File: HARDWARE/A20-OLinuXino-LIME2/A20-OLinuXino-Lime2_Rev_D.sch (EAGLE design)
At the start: 421 parts, among them Q1 E4SB25.000F20E15(25MHz/20pF/2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, Q3 4SB24.000F20E15/5x3.2mm/20ppm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, Q4 32768Hz/6pF, T1 BC846B, U1 A20, U10 SY6280, U11 SY6280, U12 SY6280, U13 AXP209(QFN48), U14 MCP120T475I-TT, U15 SY8008C(AA)C, U16 SY7208(SOT23-6), U17 SY8008C(AA)C, U18 FIDUCIAL, U19 FIDUCIAL, U2 K4B4G1646D-BCK0, U20 FIDUCIAL, U21 FIDUCIAL, U3 K4B4G1646D-BCK0, U4 H27UBG8T2BTR, U5 RTL8211CL-GR, U6 AT24C16BN-SH, U7 NA(RCLAMP0524P), U8 NA(RCLAMP0524P), U9 NA(RCLAMP0524P)

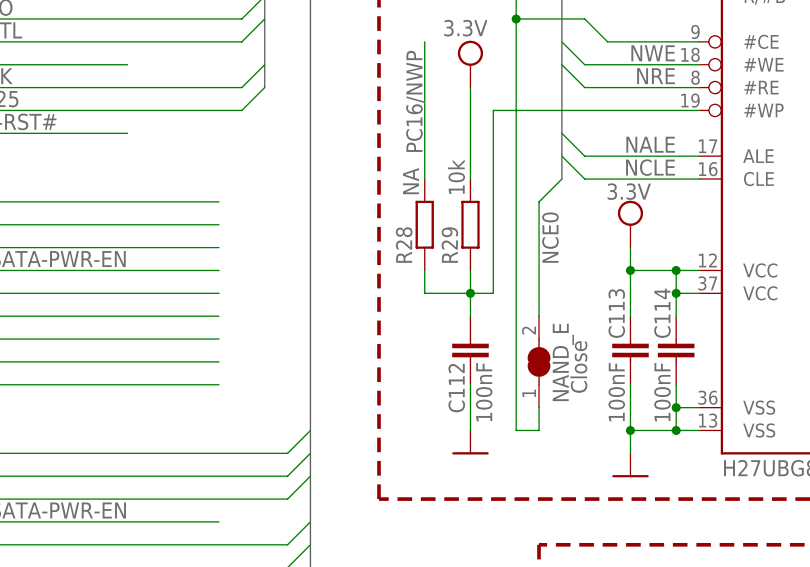
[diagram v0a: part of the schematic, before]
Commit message: Rename R28 to NAND_WP
R28 is a spot where a zero ohm resistor can be placed to control the
NAND flash's Write Protect. This commit renames this resistor to NAND_WP
and marks it as such on the silk-screen.

Signed-off-by: Olliver Schinagl <o.schinagl@ultimaker.com>
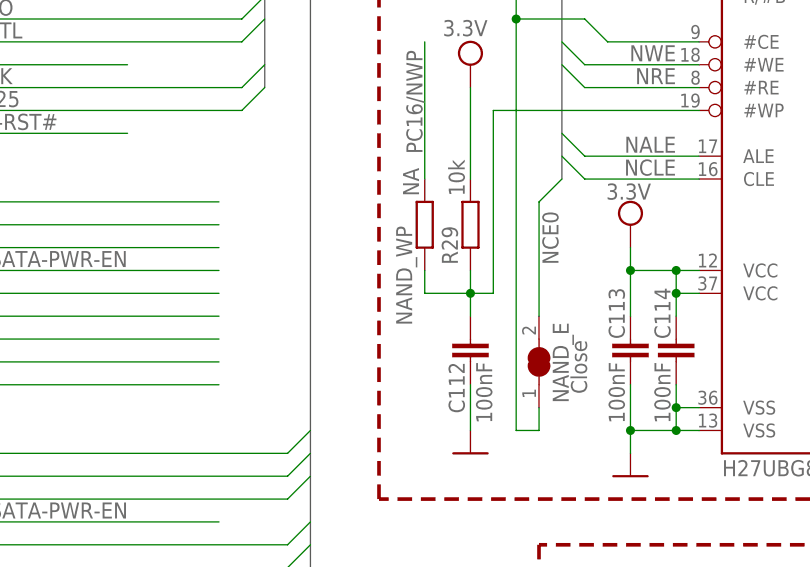
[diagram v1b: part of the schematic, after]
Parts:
- renumbered R28 to NAND_WP
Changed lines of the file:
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@@
 <?xml version="1.0" encoding="utf-8"?>
 <!DOCTYPE eagle SYSTEM "eagle.dtd">
-<eagle version="6.6.0">
+<eagle version="7.2.0">
 <drawing>
 <settings>
@@
 <part name="P+12" library="supply1" deviceset="+5V" device=""/>
 <part name="GND61" library="supply1" deviceset="GND" device="" value=""/>
-<part name="R28" library="rcl" deviceset="R-EU_" device="R0402_TI" value="NA"/>
+<part name="NAND_WP" library="rcl" deviceset="R-EU_" device="R0402_TI" value="NA"/>
 <part name="LAN" library="OLIMEX_CONNECTORS" deviceset="TM211Q01FM22_SH" device=""/>
 <part name="C214" library="rcl" deviceset="C-EU" device="C1206_5MILS_WS_ISO" value="1nF/2kV/X7R/1206"/>
@@
 </instance>
 <instance part="GND61" gate="1" x="464.82" y="111.76" rot="MR0"/>
-<instance part="R28" gate="G$1" x="233.68" y="535.94" smashed="yes" rot="MR270">
+<instance part="NAND_WP" gate="G$1" x="233.68" y="535.94" smashed="yes" rot="MR270">
 <attribute name="NAME" x="232.283" y="535.813" size="1.778" layer="95" rot="MR270"/>
 <attribute name="VALUE" x="233.045" y="539.115" size="1.778" layer="96" rot="R90"/>
@@
 <pinref part="C112" gate="G$1" pin="2"/>
 <pinref part="U4" gate="G$1" pin="#WP"/>
-<pinref part="R28" gate="G$1" pin="2"/>
+<pinref part="NAND_WP" gate="G$1" pin="2"/>
 </segment>
 </net>
@@
 <wire x1="233.68" y1="541.02" x2="233.68" y2="556.26" width="0.1524" layer="91"/>
 <label x="233.426" y="543.814" size="1.778" layer="95" rot="R90"/>
-<pinref part="R28" gate="G$1" pin="1"/>
+<pinref part="NAND_WP" gate="G$1" pin="1"/>
 </segment>
 </net>
